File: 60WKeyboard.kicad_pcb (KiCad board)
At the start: 4 copper layers, 293.9 x 108.2 mm, 241 parts, among them IC2 USBLC6-2SC6, J1 USB4215-03-A_REVA, J2 Conn_02x01_MountingPin, J3 Conn_01x04_Socket, U2 TXB0101DRL, U3 nRF52840, Y1 ABM11W-32.0000MHZ-7-D1X-T3, Y2 ECS-.327-7-12-TR

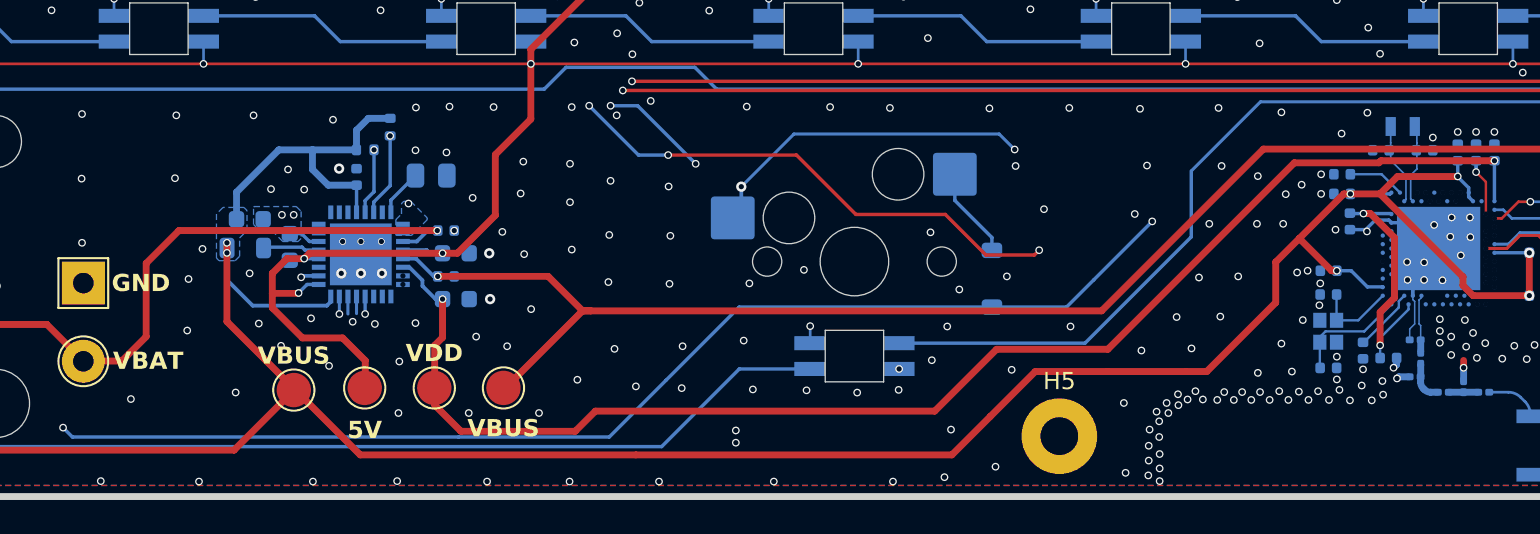
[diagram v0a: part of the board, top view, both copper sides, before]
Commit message: Add RGB power control circuit and update PCB
Introduced a new RGB power control circuit using a DMG2301L MOSFET and 10k resistor, connected to the /RGB_POWER net. Updated test point references, modified net assignments, and adjusted routing and vias in the PCB layout. Added and removed backup files and updated production files to reflect the latest design changes.
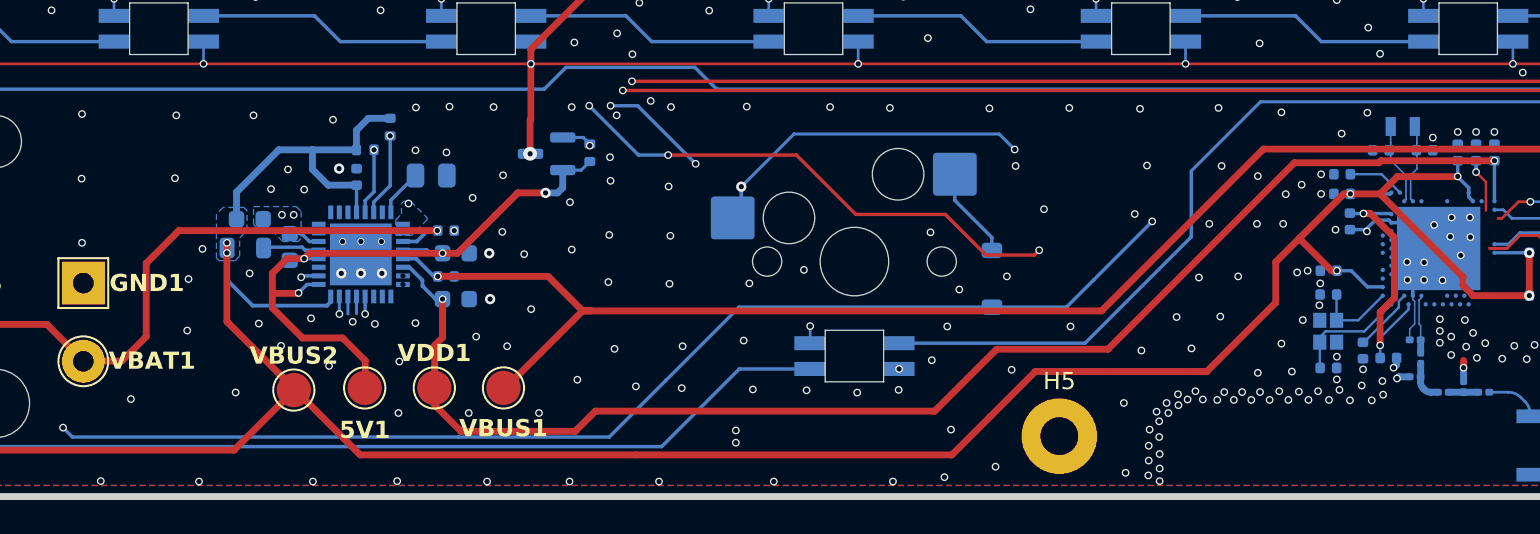
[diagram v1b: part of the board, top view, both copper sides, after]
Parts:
- added Q1: DMG2301L, Package_TO_SOT_SMD:SOT-23, B.Cu at (175.7, 166.7)
- added R9: 10k, Resistor_SMD:R_0402_1005Metric, B.Cu at (178.2, 166.6)
- renumbered 5V to 5V1, GND to GND1, VBAT to VBAT1, VBUS to VBUS1, VBUS to VBUS2, VDD to VDD1
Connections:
- U3 pad L1: unconnected-(U3-P0.06-PadL1) -> /RGB_POWER
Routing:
- net /RGB_POWER: track 0.00 -> 55.5 mm, vias 0 -> 3
- net +5V: track 1383.9 -> 1386.9 mm, vias 63 -> 65
- net GND: vias 1483 -> 1482
